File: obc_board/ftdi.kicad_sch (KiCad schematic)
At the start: 20 parts, among them U10 AP2127N-3.3, U11 FT4232H-56Q-REEL, Y1 12MHz

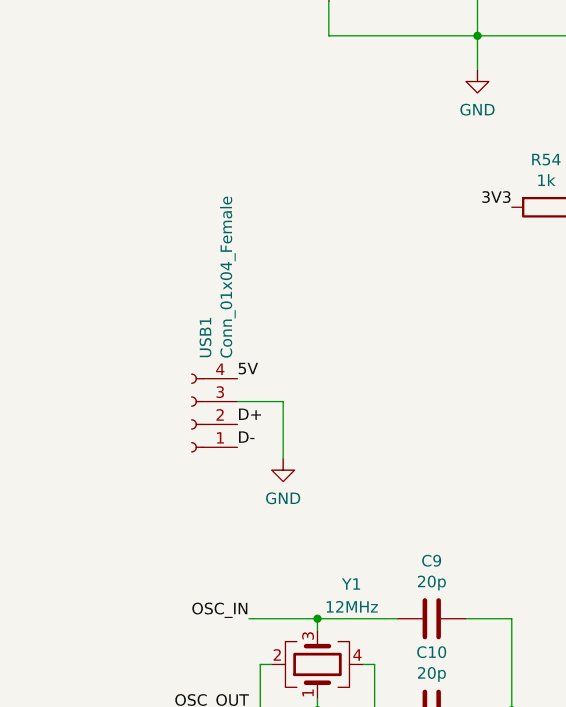
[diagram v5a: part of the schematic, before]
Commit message: changed picoblade symbols to include mounting pins, added photodiode circuitry and additional testpoints, added GPS to FTDI jumper
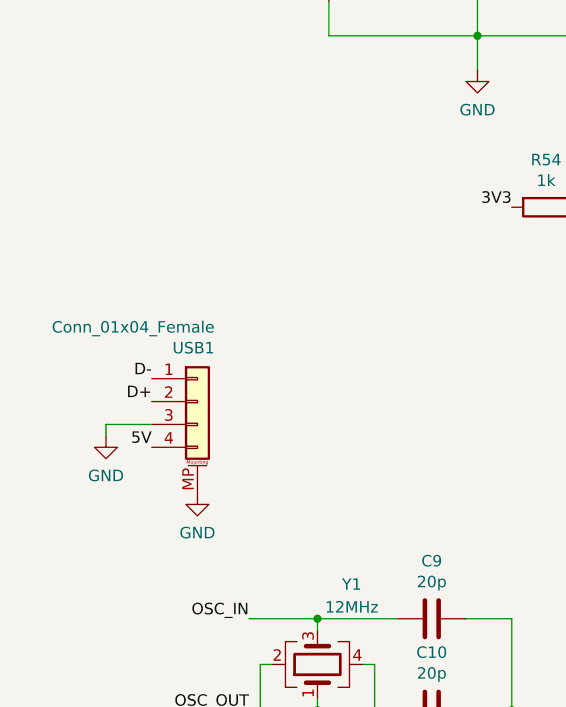
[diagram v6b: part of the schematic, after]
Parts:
- USB1: symbol Connector:Conn_01x04_Female -> Connector_Generic_MountingPin:Conn_01x04_MountingPin
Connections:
- net GND: now also USB1.MP (MountPin)
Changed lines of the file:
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@@
-    (stroke (width 0) (type default) (color 0 0 0 0))
-  )
-  (wire (pts (xy 78.74 101.6) (xy 78.74 95.25))
     (stroke (width 0) (type default) (color 0 0 0 0))
   )
@@
     (stroke (width 0) (type default) (color 0 0 0 0))
   )
+  (wire (pts (xy 59.055 97.79) (xy 64.135 97.79))
+    (stroke (width 0) (type default) (color 0 0 0 0))
+  )
   (wire (pts (xy 121.92 85.09) (xy 121.92 87.63))
     (stroke (width 0) (type default) (color 0 0 0 0))
@@
     (stroke (width 0) (type default) (color 0 0 0 0))
   )
+  (wire (pts (xy 59.055 99.06) (xy 59.055 97.79))
+    (stroke (width 0) (type default) (color 0 0 0 0))
+  )
   (wire (pts (xy 121.92 77.47) (xy 121.92 73.66))
     (stroke (width 0) (type default) (color 0 0 0 0))
@@
   )
   (wire (pts (xy 134.62 77.47) (xy 134.62 76.2))
-    (stroke (width 0) (type default) (color 0 0 0 0))
-  )
-  (wire (pts (xy 78.74 95.25) (xy 73.66 95.25))
     (stroke (width 0) (type default) (color 0 0 0 0))
   )
@@
     (effects (font (size 1.27 1.27)) (justify right bottom))
   )
-  (label "5V" (at 73.66 92.71 0)
-    (effects (font (size 1.27 1.27)) (justify left bottom))
+  (label "5V" (at 64.135 100.33 180)
+    (effects (font (size 1.27 1.27)) (justify right bottom))
   )
   (label "3V3" (at 104.14 73.66 180)
     (effects (font (size 1.27 1.27)) (justify right bottom))
   )
-  (label "D-" (at 73.66 100.33 0)
-    (effects (font (size 1.27 1.27)) (justify left bottom))
+  (label "D-" (at 64.135 92.71 180)
+    (effects (font (size 1.27 1.27)) (justify right bottom))
   )
   (label "3V3" (at 187.96 73.66 0)
@@
     (effects (font (size 1.27 1.27)) (justify left bottom))
   )
-  (label "D+" (at 73.66 97.79 0)
-    (effects (font (size 1.27 1.27)) (justify left bottom))
+  (label "D+" (at 64.135 95.25 180)
+    (effects (font (size 1.27 1.27)) (justify right bottom))
   )
   (label "D+" (at 142.24 78.74 180)
@@
     (pin "2")
   )
-  (symbol (lib_id "Connector:Conn_01x04_Female") (at 68.58 97.79 180) (unit 1)
-    (in_bom yes) (on_board yes)
-    (property "Reference" "USB1" (id 0) (at 70.1548 90.4748 90)
+  (symbol (lib_id "Connector_Generic_MountingPin:Conn_01x04_MountingPin") (at 69.215 95.25 0) (unit 1)
+    (in_bom yes) (on_board yes)
+    (property "Reference" "USB1" (id 0) (at 71.12 89.3064 0)
       (effects (font (size 1.27 1.27)) (justify right))
     )
-    (property "Value" "Conn_01x04_Female" (id 1) (at 72.4662 90.4748 90)
+    (property "Value" "Conn_01x04_Female" (id 1) (at 71.12 86.995 0)
       (effects (font (size 1.27 1.27)) (justify right))
     )
-    (property "Footprint" "Connector_Molex:Molex_PicoBlade_53261-0471_1x04-1MP_P1.25mm_Horizontal" (id 2) (at 68.58 97.79 0)
-      (effects (font (size 1.27 1.27)) hide)
-    )
-    (property "Datasheet" "~" (id 3) (at 68.58 97.79 0)
-      (effects (font (size 1.27 1.27)) hide)
-    )
-    (property "Digikey Part Number" "WM7622CT-ND" (id 4) (at 68.58 97.79 0)
+    (property "Footprint" "Connector_Molex:Molex_PicoBlade_53261-0471_1x04-1MP_P1.25mm_Horizontal" (id 2) (at 69.215 95.25 0)
+      (effects (font (size 1.27 1.27)) hide)
+    )
+    (property "Datasheet" "~" (id 3) (at 69.215 95.25 0)
+      (effects (font (size 1.27 1.27)) hide)
+    )
+    (property "Digikey Part Number" "WM7622CT-ND" (id 4) (at 69.215 95.25 0)
       (effects (font (size 1.27 1.27)) hide)
     )
@@
     (pin "3")
     (pin "4")
+    (pin "MP")
   )
   (symbol (lib_id "Regulator_Linear:AP2127N-3.3") (at 100.33 41.91 0) (unit 1)
@@
     (pin "1")
   )
+  (symbol (lib_id "power:GND") (at 59.055 99.06 0) (unit 1)
+    (in_bom yes) (on_board yes) (fields_autoplaced)
+    (property "Reference" "#PWR?" (id 0) (at 59.055 105.41 0)
+      (effects (font (size 1.27 1.27)) hide)
+    )
+    (property "Value" "GND" (id 1) (at 59.055 103.5034 0))
+    (property "Footprint" "" (id 2) (at 59.055 99.06 0)
+      (effects (font (size 1.27 1.27)) hide)
+    )
+    (property "Datasheet" "" (id 3) (at 59.055 99.06 0)
+      (effects (font (size 1.27 1.27)) hide)
+    )
+    (pin "1")
+  )
   (symbol (lib_id "Device:Crystal_GND24") (at 82.55 124.46 90) (unit 1)
     (in_bom yes) (on_board yes)
@@
     (pin "1")
   )
-  (symbol (lib_id "power:GND") (at 78.74 101.6 0) (unit 1)
-    (in_bom yes) (on_board yes) (fields_autoplaced)
-    (property "Reference" "#PWR024" (id 0) (at 78.74 107.95 0)
-      (effects (font (size 1.27 1.27)) hide)
-    )
-    (property "Value" "GND" (id 1) (at 78.74 106.0434 0))
-    (property "Footprint" "" (id 2) (at 78.74 101.6 0)
-      (effects (font (size 1.27 1.27)) hide)
-    )
-    (property "Datasheet" "" (id 3) (at 78.74 101.6 0)
-      (effects (font (size 1.27 1.27)) hide)
-    )
-    (pin "1")
-  )
   (symbol (lib_id "power:GND") (at 190.5 157.48 0) (unit 1)
     (in_bom yes) (on_board yes) (fields_autoplaced)
@@
       (effects (font (size 1.27 1.27)) hide)
     )
+    (pin "1")
+  )
+  (symbol (lib_id "power:GND") (at 69.215 105.41 0) (unit 1)
+    (in_bom yes) (on_board yes) (fields_autoplaced)
+    (property "Reference" "#PWR?" (id 0) (at 69.215 111.76 0)
+      (effects (font (size 1.27 1.27)) hide)
+    )
+    (property "Value" "GND" (id 1) (at 69.215 109.8534 0))
+    (property "Footprint" "" (id 2) (at 69.215 105.41 0)
+      (effects (font (size 1.27 1.27)) hide)
+    )
+    (property "Datasheet" "" (id 3) (at 69.215 105.41 0)
+      (effects (font (size 1.27 1.27)) hide)
+    )
